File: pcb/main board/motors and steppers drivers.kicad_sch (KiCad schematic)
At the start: 35 parts, among them J1 Motor 0 Conn, J2 Motor 1 Conn, J3 Motor 2 Conn, J4 Motor 3 Conn, J7 Stepper 1 Conn, J8 Stepper 2 Conn, J9 Stepper 3 Conn, U1 L298HN, U2 L298HN

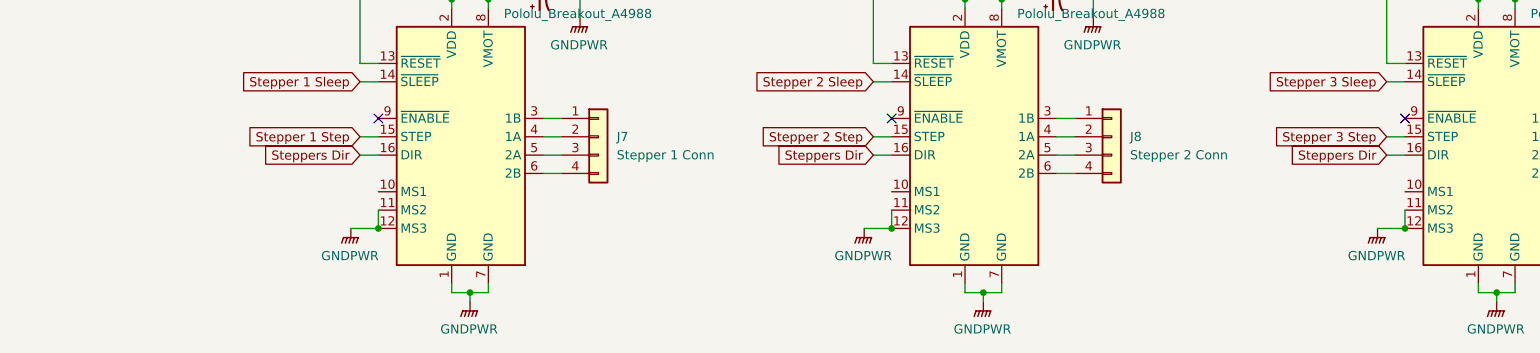
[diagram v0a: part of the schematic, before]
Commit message: Added Jumpers To select Steppers speed
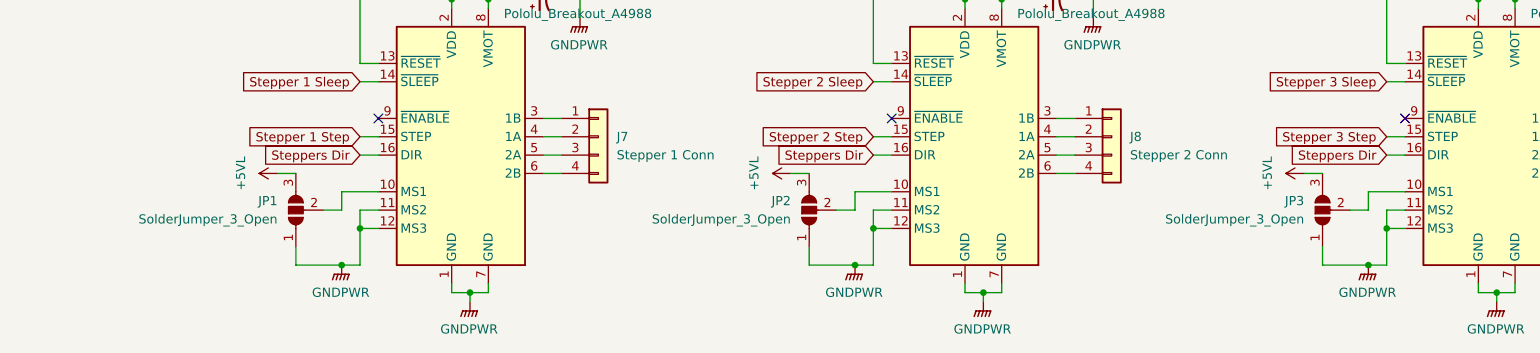
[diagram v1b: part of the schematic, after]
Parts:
- added JP1, JP2, JP3: SolderJumper_3_Open, Jumper:SolderJumper-3_P1.3mm_Open_RoundedPad1.0x1.5mm, symbol Jumper:SolderJumper_3_Open
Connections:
- net +5VL: now also JP1.3 (B), JP2.3 (B), JP3.3 (B)
- net GNDPWR: now also JP1.1 (A), JP2.1 (A), JP3.1 (A)
- net at A5.10 (MS1): now also JP3.2 (C)
- net at A3.10 (MS1): now also JP1.2 (C)
- net at A4.10 (MS1): now also JP2.2 (C)

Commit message: Finished correcting and updating footprints for capacitors and started to change connectors footprints
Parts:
- J1, J2, J3, J4: footprint Connector_PinHeader_2.54mm:PinHeader_1x02_P2.54mm_Vertical -> Connector_Molex:Molex_KK-254_AE-6410-02A_1x02_P2.54mm_Vertical
- J7, J8, J9: footprint Connector_PinHeader_2.54mm:PinHeader_1x04_P2.54mm_Vertical -> Connector_Molex:Molex_KK-254_AE-6410-04A_1x04_P2.54mm_Vertical
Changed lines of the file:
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@@
 			)
 		)
-		(property "Footprint" "Connector_PinHeader_2.54mm:PinHeader_1x02_P2.54mm_Vertical"
+		(property "Footprint" "Connector_Molex:Molex_KK-254_AE-6410-02A_1x02_P2.54mm_Vertical"
 			(at 127 53.34 0)
 			(effects
@@
 			)
 		)
-		(property "Footprint" "Connector_PinHeader_2.54mm:PinHeader_1x02_P2.54mm_Vertical"
+		(property "Footprint" "Connector_Molex:Molex_KK-254_AE-6410-02A_1x02_P2.54mm_Vertical"
 			(at 259.08 53.34 0)
 			(effects
@@
 			)
 		)
-		(property "Footprint" "Connector_PinHeader_2.54mm:PinHeader_1x04_P2.54mm_Vertical"
+		(property "Footprint" "Connector_Molex:Molex_KK-254_AE-6410-04A_1x04_P2.54mm_Vertical"
 			(at 99.06 128.27 0)
 			(effects
@@
 			)
 		)
-		(property "Footprint" "Connector_PinHeader_2.54mm:PinHeader_1x04_P2.54mm_Vertical"
+		(property "Footprint" "Connector_Molex:Molex_KK-254_AE-6410-04A_1x04_P2.54mm_Vertical"
 			(at 170.18 128.27 0)
 			(effects
@@
 			)
 		)
-		(property "Footprint" "Connector_PinHeader_2.54mm:PinHeader_1x02_P2.54mm_Vertical"
+		(property "Footprint" "Connector_Molex:Molex_KK-254_AE-6410-02A_1x02_P2.54mm_Vertical"
 			(at 127 60.96 0)
 			(effects
@@
 			)
 		)
-		(property "Footprint" "Connector_PinHeader_2.54mm:PinHeader_1x02_P2.54mm_Vertical"
+		(property "Footprint" "Connector_Molex:Molex_KK-254_AE-6410-02A_1x02_P2.54mm_Vertical"
 			(at 259.08 60.96 0)
 			(effects
@@
 			)
 		)
-		(property "Footprint" "Connector_PinHeader_2.54mm:PinHeader_1x04_P2.54mm_Vertical"
+		(property "Footprint" "Connector_Molex:Molex_KK-254_AE-6410-04A_1x04_P2.54mm_Vertical"
 			(at 241.3 128.27 0)
 			(effects
